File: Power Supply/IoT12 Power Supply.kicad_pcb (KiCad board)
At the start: 2 copper layers, 91.4 x 73.7 mm, 16 parts, among them J1 Screw_Terminal_01x03, J2 Screw_Terminal_01x03

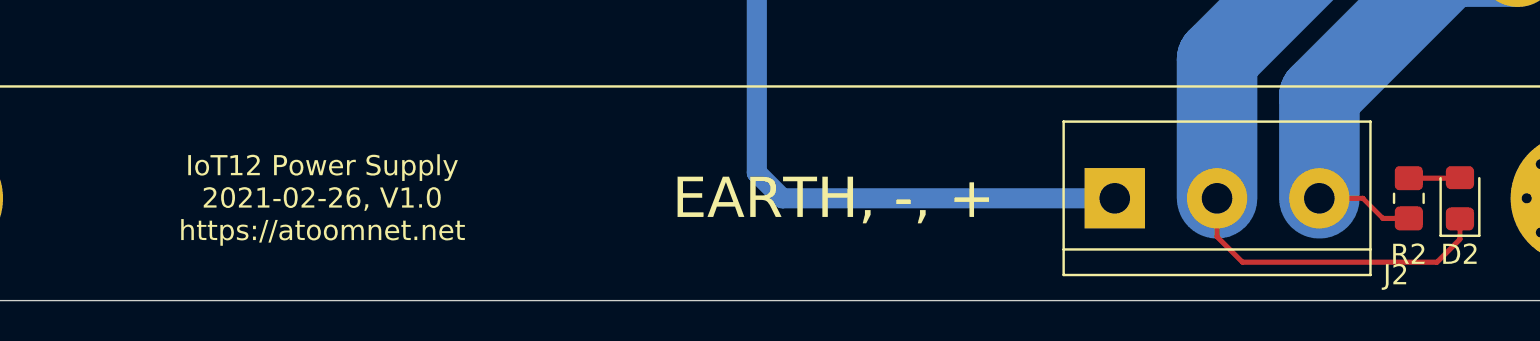
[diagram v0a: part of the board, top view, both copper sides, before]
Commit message: Add: this PCB is not safe to use.
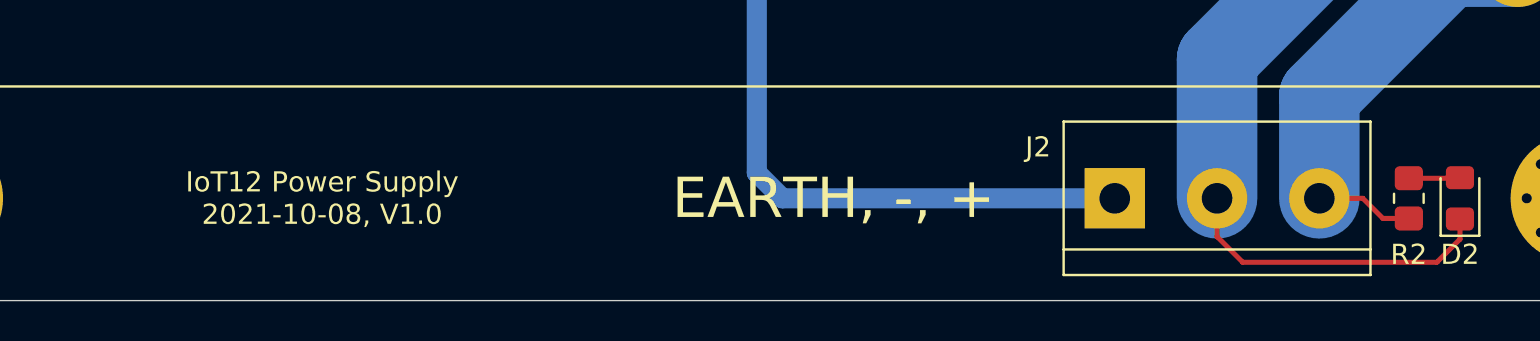
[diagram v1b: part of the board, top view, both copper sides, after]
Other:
- board text added: "IoT12 Power Supply 2021-10-08, V1.0"
- board text added: "This PCB is not safe to use. Use at your own risk. When powered on it becomes deadly when touched or could set your house on fire when left unsupervised."
- board text removed: "IoT12 Power Supply 2021-02-26, V1.0 https://atoomnet.net"

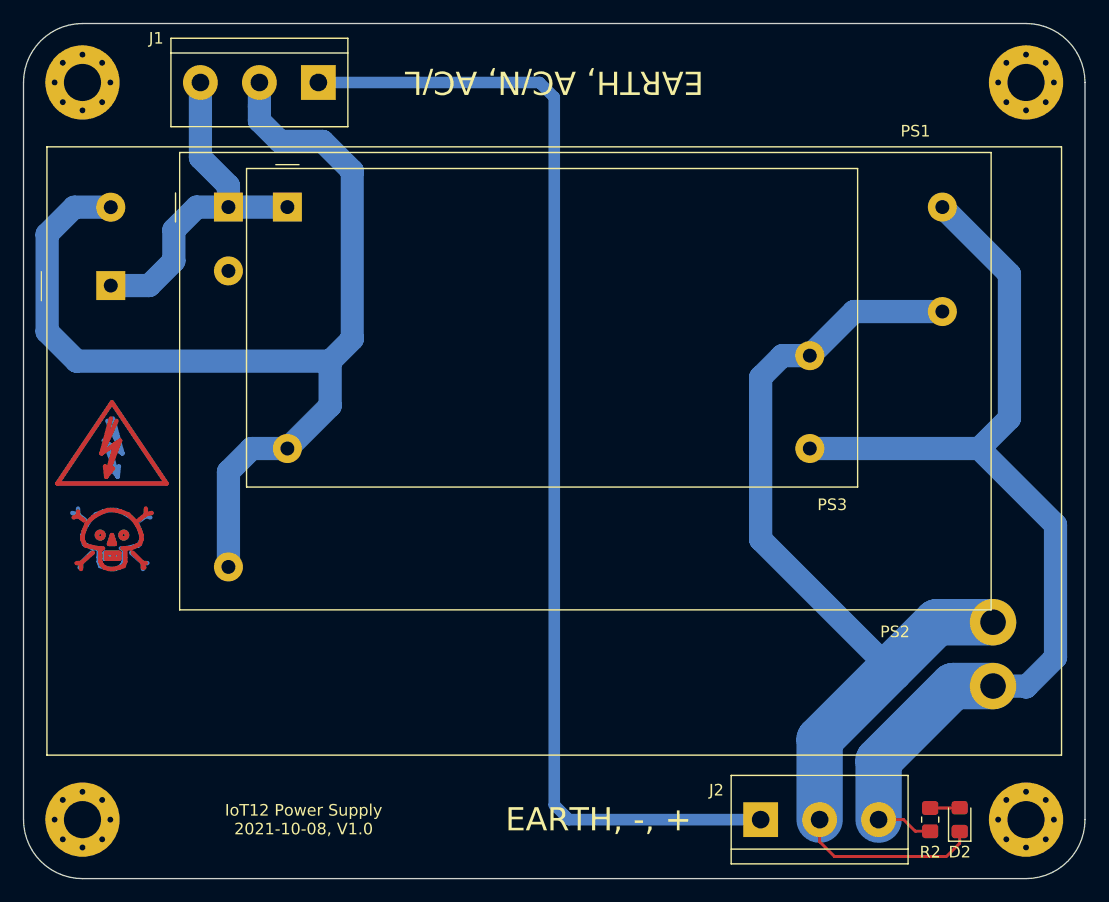
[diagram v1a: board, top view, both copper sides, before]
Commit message: Remove all lower power supply options.
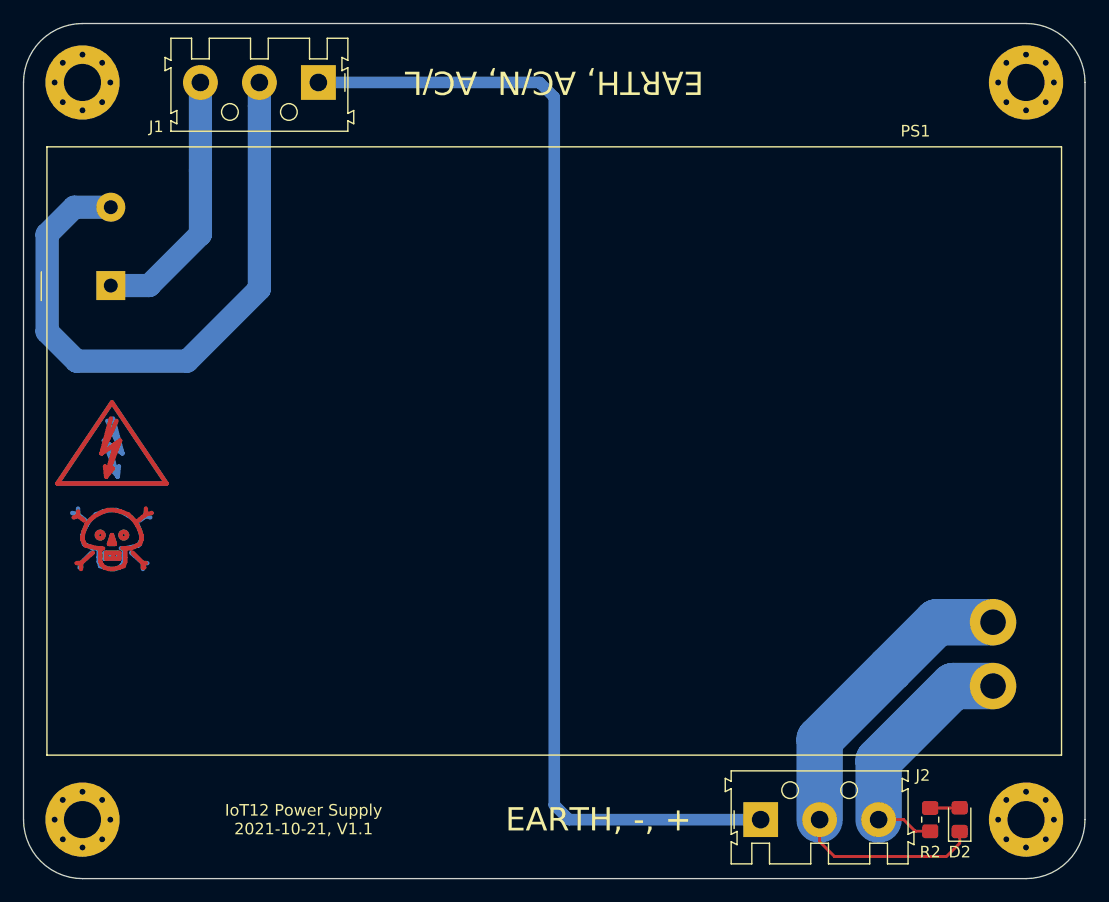
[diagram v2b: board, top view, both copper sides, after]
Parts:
- removed PS2: MPM-30-15*, Converter-ACDC-extra:Converter_ACDC_MeanWell_MPM-30-xx_THT
- removed PS3: MPM-20-12*, Converter-ACDC-extra:Converter_ACDC_MeanWell_MPM-20-xx_THT
- J1, J2: footprint TerminalBlock:TerminalBlock_bornier-3_P5.08mm -> TerminalBlock-extra:TerminalBlock_Weidmueller-PM-5.08-03-90-3.5SN-BK-BX
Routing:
- net /Vout+: track 88.5 -> 22.5 mm
- net /Vout-: track 89.7 -> 42.0 mm
- net /N: track 93.7 -> 54.5 mm
- net /L: track 31.3 -> 22.6 mm
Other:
- board text added: "IoT12 Power Supply 2021-10-21, V1.1"
- board text added: "Recommended power supply module: Mean Well MPM-90-24 Input: 80-264VAC, 113-370VDC. Output: 24V, 3.75A, 90W. https://github.com/atoomnetmarc/IoT12-hardware Apache License, Version 2.0"
- board text removed: "IoT12 Power Supply 2021-10-08, V1.0"
- board text removed: "Recommended power supply module: Mean Well MPM-90-24 Input: 80-264VAC, 113-370VDC. Output: 24V, 3.75A, 90W. Lower power alternatives: Mean Well MPM-30-15 Input: 80-264VAC. Output: 15V, 2.3A, 30W. Mean Well MPM-20-12 Input: 80-264VAC, 113V-370VDC. Output: 12V, 1.8A, 21.6W. https://github.com/atoomnetmarc/IoT12-hardware Apache License, Version 2.0"
